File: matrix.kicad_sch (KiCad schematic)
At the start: 150 parts, among them SW10 SW_Push, SW11 SW_Push, SW12 SW_Push, SW13 SW_Push, SW14 SW_Push, SW15 SW_Push, SW16 SW_Push, SW17 SW_Push, SW18 SW_Push, SW19 SW_Push, SW2 SW_Push, SW20 SW_Push, SW21 SW_Push, SW22 SW_Push, SW23 SW_Push, SW24 SW_Push, SW25 SW_Push, SW26 SW_Push, SW27 SW_Push, SW28 SW_Push, SW29 SW_Push, SW3 SW_Push, SW30 SW_Push, SW31 SW_Push, SW32 SW_Push, SW33 SW_Push, SW34 SW_Push, SW35 SW_Push, SW36 SW_Push, SW37 SW_Push, SW38 SW_Push, SW39 SW_Push, SW4 SW_Push, SW40 SW_Push, SW41 SW_Push, SW42 SW_Push, SW43 SW_Push, SW44 SW_Push, SW45 SW_Push, SW46 SW_Push, SW47 SW_Push, SW48 SW_Push, SW49 SW_Push, SW5 SW_Push, SW50 SW_Push, SW51 SW_Push, SW52 SW_Push, SW53 SW_Push, SW54 SW_Push, SW55 SW_Push, SW56 SW_Push, SW57 SW_Push, SW58 SW_Push, SW59 SW_Push, SW6 SW_Push, SW60 SW_Push, SW61 SW_Push, SW62 SW_Push, SW63 SW_Push, SW64 SW_Push, SW65 SW_Push, SW66 SW_Push, SW67 SW_Push, SW68 SW_Push, SW69 SW_Push, SW7 SW_Push, SW70 SW_Push, SW71 SW_Push, SW72 SW_Push, SW73 SW_Push, SW74 SW_Push, SW75 SW_Push, SW76 SW_Push, SW8 SW_Push, SW9 SW_Push

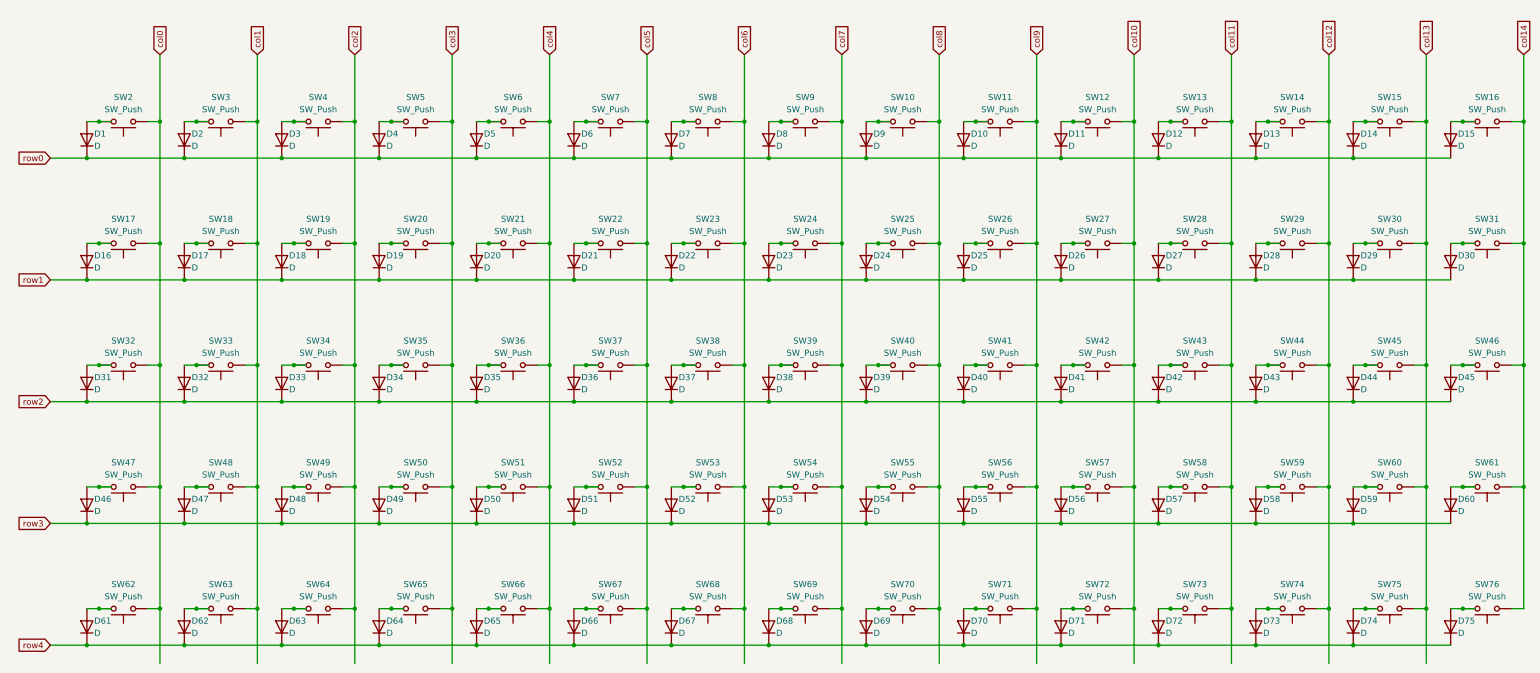
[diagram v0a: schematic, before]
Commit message: Matrix Design and slight keycap config
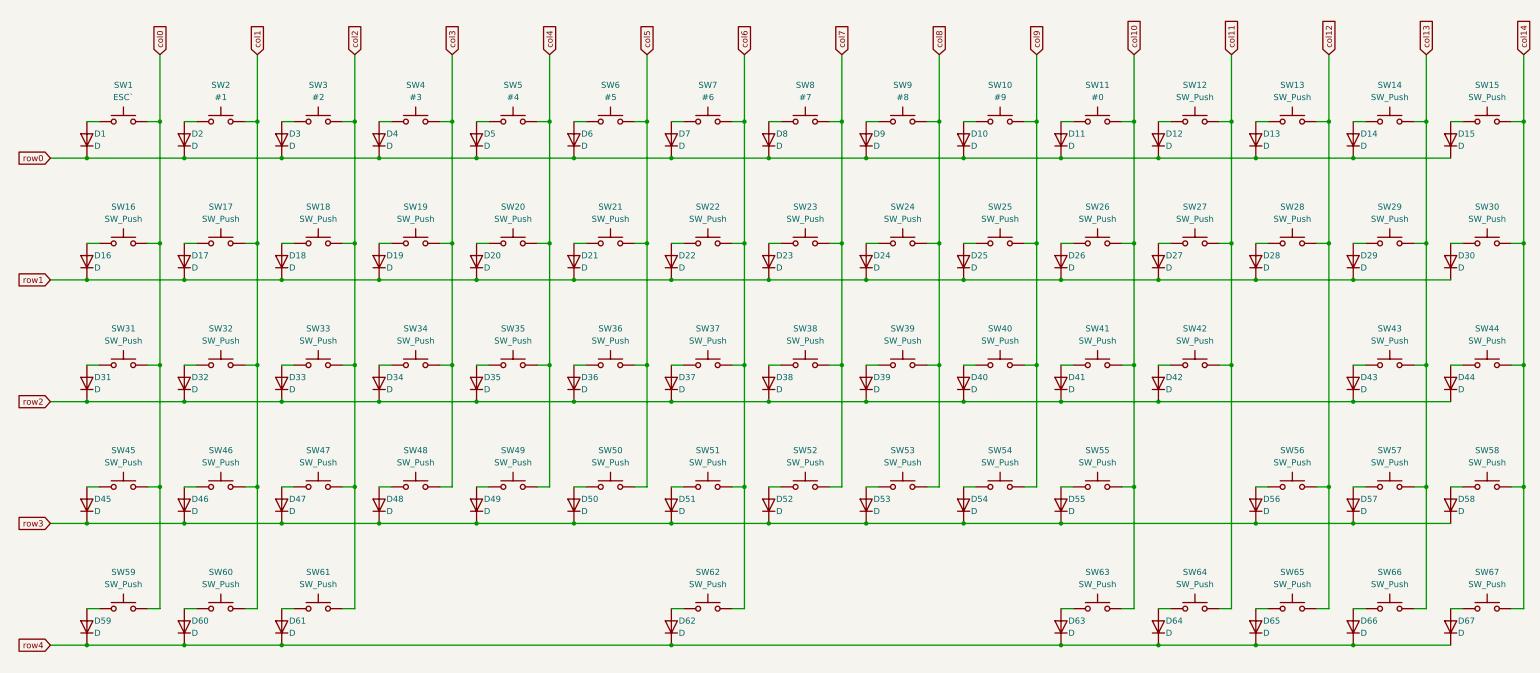
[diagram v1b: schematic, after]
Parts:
- removed D68, D69, D70, D71, D72, D73, D74, D75: D, symbol Device:D
- removed SW68, SW69, SW70, SW71, SW72, SW73, SW74, SW75, SW76: SW_Push, symbol Switch:SW_Push
- added SW2: #1, symbol Switch:SW_Push
- SW1: renamed from SW2; value SW_Push -> ESC`
- SW10: value SW_Push -> #9
- SW11: value SW_Push -> #0
- SW3: value SW_Push -> #2
- SW4: value SW_Push -> #3
- SW5: value SW_Push -> #4
- SW6: value SW_Push -> #5
- SW7: value SW_Push -> #6
- SW8: value SW_Push -> #7
- SW9: value SW_Push -> #8
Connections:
- net col0: now also SW1.2, SW16.2, SW31.2, SW45.2, SW59.2; no longer SW1.1, SW17.1, SW32.1, SW47.1, SW62.1
- net col1: now also SW17.2, SW32.2, SW46.2, SW60.2, SW2.2; no longer SW18.1, SW3.1, SW33.1, SW48.1, SW63.1
- net col10: now also SW11.2, SW26.2, SW41.2, SW55.2, SW63.2; no longer SW12.1, SW27.1, SW42.1, SW57.1
- net col11: now also SW12.2, SW27.2, SW42.2, SW64.2; no longer SW13.1, SW28.1, SW43.1, SW58.1
- net col12: now also SW13.2, SW28.2, SW56.2, SW65.2; no longer SW14.1, SW29.1, SW44.1, SW59.1
- net col13: now also SW14.2, SW29.2, SW43.2, SW57.2, SW66.2; no longer SW15.1, SW30.1, SW45.1, SW60.1
- net col14: now also SW15.2, SW30.2, SW44.2, SW58.2, SW67.2; no longer SW16.1, SW31.1, SW46.1, SW61.1
- net col2: now also SW18.2, SW3.2, SW33.2, SW47.2, SW61.2; no longer SW19.1, SW34.1, SW4.1, SW49.1, SW64.1
- net col3: now also SW19.2, SW34.2, SW4.2, SW48.2; no longer SW20.1, SW35.1, SW5.1, SW50.1, SW65.1
- net col4: now also SW20.2, SW35.2, SW49.2, SW5.2; no longer SW21.1, SW36.1, SW51.1, SW6.1, SW66.1
- net col5: now also SW21.2, SW36.2, SW50.2, SW6.2; no longer SW22.1, SW37.1, SW52.1, SW67.1, SW7.1
- net col6: now also SW22.2, SW37.2, SW51.2, SW62.2, SW7.2; no longer SW23.1, SW38.1, SW53.1, SW8.1
- net col7: now also SW23.2, SW38.2, SW52.2, SW8.2; no longer SW24.1, SW39.1, SW54.1, SW9.1
- net col8: now also SW24.2, SW39.2, SW53.2, SW9.2; no longer SW10.1, SW25.1, SW40.1, SW55.1
- net col9: now also SW10.2, SW25.2, SW40.2, SW54.2; no longer SW11.1, SW26.1, SW41.1, SW56.1
- net row2: no longer D45.1 (K)
- net row3: now also D45.1 (K); no longer D59.1 (K), D60.1 (K)
- net row4: now also D59.1 (K), D60.1 (K)
- net at D49.2 (A): now also SW49.1; no longer SW50.2
- net at D14.2 (A): now also SW14.1; no longer SW15.2
- net at D15.2 (A): now also SW15.1; no longer SW16.2
- net at D50.2 (A): now also SW50.1; no longer SW51.2
- net at D65.2 (A): now also SW65.1; no longer SW66.2
- net at D16.2 (A): now also SW16.1; no longer SW17.2
- net at D63.2 (A): now also SW63.1; no longer SW64.2
- net at D45.2 (A): now also SW45.1; no longer SW46.2
- net at D30.2 (A): now also SW30.1; no longer SW31.2
- net at D56.2 (A): now also SW56.1; no longer SW57.2
- net at D7.2 (A): now also SW7.1; no longer SW8.2
- net at D5.2 (A): now also SW5.1; no longer SW6.2
- net at D43.2 (A): now also SW43.1; no longer SW44.2
- net at D33.2 (A): now also SW33.1; no longer SW34.2
- net at D19.2 (A): now also SW19.1; no longer SW20.2
- net at D27.2 (A): now also SW27.1; no longer SW28.2
- net at D17.2 (A): now also SW17.1; no longer SW18.2
- net at D57.2 (A): now also SW57.1; no longer SW58.2
- net at D39.2 (A): now also SW39.1; no longer SW40.2
- net at D4.2 (A): now also SW4.1; no longer SW5.2
- net at D18.2 (A): now also SW18.1; no longer SW19.2
- net at D9.2 (A): now also SW9.1; no longer SW10.2
- net at D42.2 (A): now also SW42.1; no longer SW43.2
- net at D59.2 (A): now also SW59.1; no longer SW60.2
- net at D40.2 (A): now also SW40.1; no longer SW41.2
- net at D6.2 (A): now also SW6.1; no longer SW7.2
- net at D55.2 (A): now also SW55.1; no longer SW56.2
- net at D44.2 (A): now also SW44.1; no longer SW45.2
- net at D1.2 (A): now also SW1.1; no longer SW1.2
- net at D66.2 (A): now also SW66.1; no longer SW67.2
- net at D11.2 (A): now also SW11.1; no longer SW12.2
- net at D62.2 (A): now also SW62.1; no longer SW63.2
- net at D52.2 (A): now also SW52.1; no longer SW53.2
- net at D26.2 (A): now also SW26.1; no longer SW27.2
- net at D29.2 (A): now also SW29.1; no longer SW30.2
- net at D2.2 (A): now also SW2.1; no longer SW3.2
- net at D12.2 (A): now also SW12.1; no longer SW13.2
- net at D60.2 (A): now also SW60.1; no longer SW61.2
- net at D38.2 (A): now also SW38.1; no longer SW39.2
- net at D67.2 (A): now also SW67.1
- net at D28.2 (A): now also SW28.1; no longer SW29.2
- net at D20.2 (A): now also SW20.1; no longer SW21.2
- net at D36.2 (A): now also SW36.1; no longer SW37.2
- net at D31.2 (A): now also SW31.1; no longer SW32.2
- net at D21.2 (A): now also SW21.1; no longer SW22.2
- net at D3.2 (A): now also SW3.1; no longer SW4.2
- net at D47.2 (A): now also SW47.1; no longer SW48.2
- net at D25.2 (A): now also SW25.1; no longer SW26.2
- net at D48.2 (A): now also SW48.1; no longer SW49.2
- net at D13.2 (A): now also SW13.1; no longer SW14.2
- net at D41.2 (A): now also SW41.1; no longer SW42.2
- net at D37.2 (A): now also SW37.1; no longer SW38.2
- net at D24.2 (A): now also SW24.1; no longer SW25.2
- net at D64.2 (A): now also SW64.1; no longer SW65.2
- net at D34.2 (A): now also SW34.1; no longer SW35.2
- net at D35.2 (A): now also SW35.1; no longer SW36.2
- net at D10.2 (A): now also SW10.1; no longer SW11.2
- net at D54.2 (A): now also SW54.1; no longer SW55.2
- net at D61.2 (A): now also SW61.1; no longer SW62.2
- net at D46.2 (A): now also SW46.1; no longer SW47.2
- net at D22.2 (A): now also SW22.1; no longer SW23.2
- net at D51.2 (A): now also SW51.1; no longer SW52.2
- net at D8.2 (A): now also SW8.1; no longer SW9.2
- net at D58.2 (A): now also SW58.1; no longer SW59.2
- net at D23.2 (A): now also SW23.1; no longer SW24.2
- net at D32.2 (A): now also SW32.1; no longer SW33.2
- net at D53.2 (A): now also SW53.1; no longer SW54.2
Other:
- moved on the sheet: SW1

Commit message: Matrix Design Done
still need to assign footprints
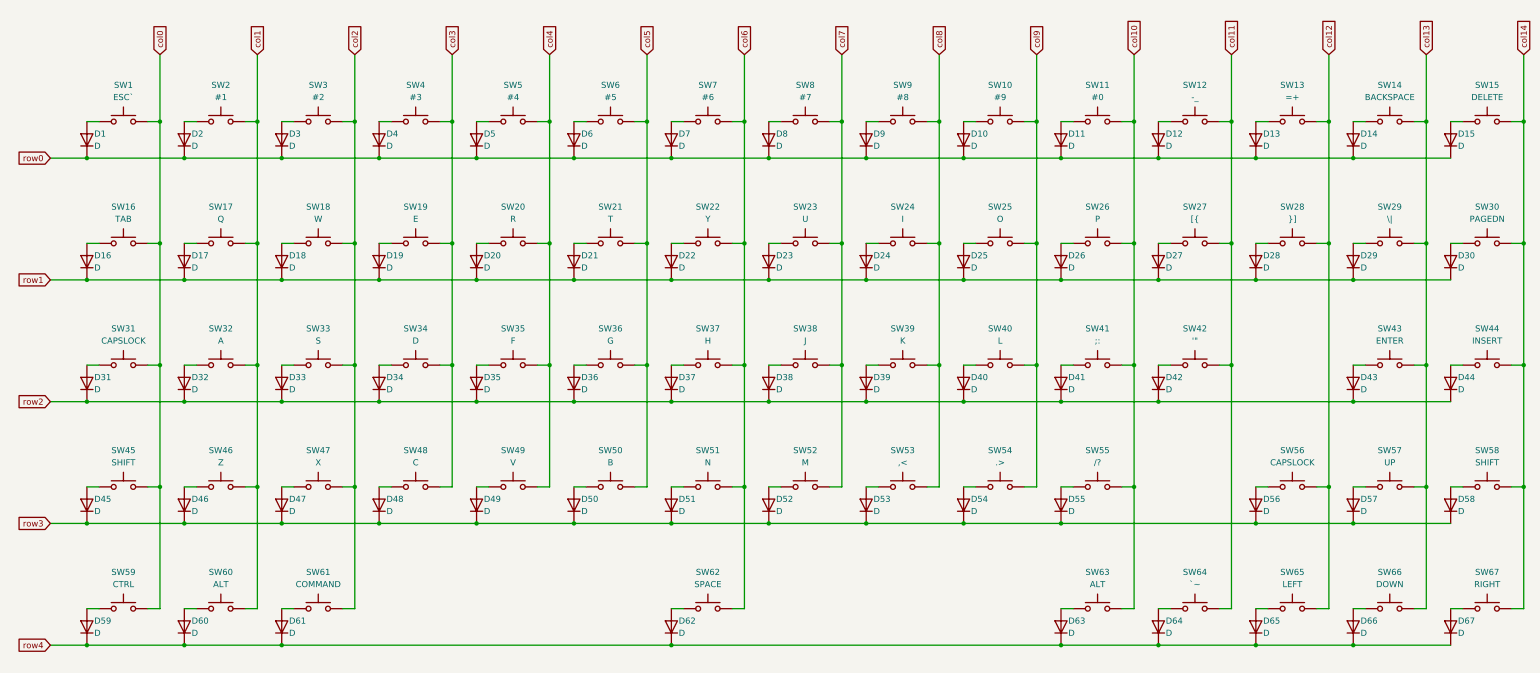
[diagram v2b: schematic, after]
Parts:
- SW12: value SW_Push -> -_
- SW13: value SW_Push -> =+
- SW14: value SW_Push -> BACKSPACE
- SW15: value SW_Push -> DELETE
- SW16: value SW_Push -> TAB
- SW17: value SW_Push -> Q
- SW18: value SW_Push -> W
- SW19: value SW_Push -> E
- SW20: value SW_Push -> R
- SW21: value SW_Push -> T
- SW22: value SW_Push -> Y
- SW23: value SW_Push -> U
- SW24: value SW_Push -> I
- SW25: value SW_Push -> O
- SW26: value SW_Push -> P
- SW27: value SW_Push -> [{
- SW28: value SW_Push -> }]
- SW29: value SW_Push -> \|
- SW30: value SW_Push -> PAGEDN
- SW31, SW56: value SW_Push -> CAPSLOCK
- SW32: value SW_Push -> A
- SW33: value SW_Push -> S
- SW34: value SW_Push -> D
- SW35: value SW_Push -> F
- SW36: value SW_Push -> G
- SW37: value SW_Push -> H
- SW38: value SW_Push -> J
- SW39: value SW_Push -> K
- SW40: value SW_Push -> L
- SW41: value SW_Push -> ;:
- SW42: value SW_Push -> '"
- SW43: value SW_Push -> ENTER
- SW44: value SW_Push -> INSERT
- SW45, SW58: value SW_Push -> SHIFT
- SW46: value SW_Push -> Z
- SW47: value SW_Push -> X
- SW48: value SW_Push -> C
- SW49: value SW_Push -> V
- SW50: value SW_Push -> B
- SW51: value SW_Push -> N
- SW52: value SW_Push -> M
- SW53: value SW_Push -> ,<
- SW54: value SW_Push -> .>
- SW55: value SW_Push -> /?
- SW57: value SW_Push -> UP
- SW59: value SW_Push -> CTRL
- SW60, SW63: value SW_Push -> ALT
- SW61: value SW_Push -> COMMAND
- SW62: value SW_Push -> SPACE
- SW64: value SW_Push -> `~
- SW65: value SW_Push -> LEFT
- SW66: value SW_Push -> DOWN
- SW67: value SW_Push -> RIGHT
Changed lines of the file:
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@@
 			)
 		)
-		(property "Value" "SW_Push"
+		(property "Value" "PAGEDN"
 			(at 341.63 67.31 0)
 			(effects
@@
 			)
 		)
-		(property "Value" "SW_Push"
+		(property "Value" "E"
 			(at 118.11 67.31 0)
 			(effects
@@
 			)
 		)
-		(property "Value" "SW_Push"
+		(property "Value" "Z"
 			(at 77.47 118.11 0)
 			(effects
@@
 			)
 		)
-		(property "Value" "SW_Push"
+		(property "Value" "=+"
 			(at 300.99 41.91 0)
 			(effects
@@
 			)
 		)
-		(property "Value" "SW_Push"
+		(property "Value" "RIGHT"
 			(at 341.63 143.51 0)
 			(effects
@@
 			)
 		)
-		(property "Value" "SW_Push"
+		(property "Value" "I"
 			(at 219.71 67.31 0)
 			(effects
@@
 			)
 		)
-		(property "Value" "SW_Push"
+		(property "Value" "INSERT"
 			(at 341.63 92.71 0)
 			(effects
@@
 			)
 		)
-		(property "Value" "SW_Push"
+		(property "Value" "SHIFT"
 			(at 341.63 118.11 0)
 			(effects
@@
 			)
 		)
-		(property "Value" "SW_Push"
+		(property "Value" "V"
 			(at 138.43 118.11 0)
 			(effects
@@
 			)
 		)
-		(property "Value" "SW_Push"
+		(property "Value" "\\|"
 			(at 321.31 67.31 0)
 			(effects
@@
 			)
 		)
-		(property "Value" "SW_Push"
+		(property "Value" "}]"
 			(at 300.99 67.31 0)
 			(effects
@@
 			)
 		)
-		(property "Value" "SW_Push"
+		(property "Value" "SHIFT"
 			(at 57.15 118.11 0)
 			(effects
@@
 			)
 		)
-		(property "Value" "SW_Push"
+		(property "Value" "A"
 			(at 77.47 92.71 0)
 			(effects
@@
 			)
 		)
-		(property "Value" "SW_Push"
+		(property "Value" ",<"
 			(at 219.71 118.11 0)
 			(effects
@@
 			)
 		)
-		(property "Value" "SW_Push"
+		(property "Value" "J"
 			(at 199.39 92.71 0)
 			(effects
@@
 			)
 		)
-		(property "Value" "SW_Push"
+		(property "Value" "CAPSLOCK"
 			(at 57.15 92.71 0)
 			(effects
@@
 			)
 		)
-		(property "Value" "SW_Push"
+		(property "Value" "COMMAND"
 			(at 97.79 143.51 0)
 			(effects
@@
 			)
 		)
-		(property "Value" "SW_Push"
+		(property "Value" "ALT"
 			(at 260.35 143.51 0)
 			(effects
@@
 			)
 		)
-		(property "Value" "SW_Push"
+		(property "Value" "U"
 			(at 199.39 67.31 0)
 			(effects
@@
 			)
 		)
-		(property "Value" "SW_Push"
+		(property "Value" ".>"
 			(at 240.03 118.11 0)
 			(effects
@@
 			)
 		)
-		(property "Value" "SW_Push"
+		(property "Value" "L"
 			(at 240.03 92.71 0)
 			(effects
@@
 			)
 		)
-		(property "Value" "SW_Push"
+		(property "Value" "ENTER"
 			(at 321.31 92.71 0)
 			(effects
@@
 			)
 		)
-		(property "Value" "SW_Push"
+		(property "Value" "TAB"
 			(at 57.15 67.31 0)
 			(effects
@@
 			)
 		)
-		(property "Value" "SW_Push"
+		(property "Value" "W"
 			(at 97.79 67.31 0)
 			(effects
@@
 			)
 		)
-		(property "Value" "SW_Push"
+		(property "Value" "S"
 			(at 97.79 92.71 0)
 			(effects
@@
 			)
 		)
-		(property "Value" "SW_Push"
+		(property "Value" "[{"
 			(at 280.67 67.31 0)
 			(effects
@@
 			)
 		)
-		(property "Value" "SW_Push"
+		(property "Value" "Q"
 			(at 77.47 67.31 0)
 			(effects
@@
 			)
 		)
-		(property "Value" "SW_Push"
+		(property "Value" "UP"
 			(at 321.31 118.11 0)
 			(effects
@@
 			)
 		)
-		(property "Value" "SW_Push"
+		(property "Value" "'\""
 			(at 280.67 92.71 0)
 			(effects
@@
 			)
 		)
-		(property "Value" "SW_Push"
+		(property "Value" "F"
 			(at 138.43 92.71 0)
 			(effects
@@
 			)
 		)
-		(property "Value" "SW_Push"
+		(property "Value" "T"
 			(at 158.75 67.31 0)
 			(effects
@@
 			)
 		)
-		(property "Value" "SW_Push"
+		(property "Value" ";:"
 			(at 260.35 92.71 0)
 			(effects
@@
 			)
 		)
-		(property "Value" "SW_Push"
+		(property "Value" "DOWN"
 			(at 321.31 143.51 0)
 			(effects
@@
 			)
 		)
-		(property "Value" "SW_Push"
+		(property "Value" "LEFT"
 			(at 300.99 143.51 0)
 			(effects
@@
 			)
 		)
-		(property "Value" "SW_Push"
+		(property "Value" "-_"
 			(at 280.67 41.91 0)
 			(effects
@@
 			)
 		)
-		(property "Value" "SW_Push"
+		(property "Value" "M"
 			(at 199.39 118.11 0)
 			(effects
@@
 			)
 		)
-		(property "Value" "SW_Push"
+		(property "Value" "CAPSLOCK"
 			(at 300.99 118.11 0)
 			(effects
@@
 			)
 		)
-		(property "Value" "SW_Push"
+		(property "Value" "B"
 			(at 158.75 118.11 0)
 			(effects
@@
 			)
 		)
-		(property "Value" "SW_Push"
+		(property "Value" "BACKSPACE"
 			(at 321.31 41.91 0)
 			(effects
@@
 			)
 		)
-		(property "Value" "SW_Push"
+		(property "Value" "K"
 			(at 219.71 92.71 0)
 			(effects
@@
 			)
 		)
-		(property "Value" "SW_Push"
+		(property "Value" "CTRL"
 			(at 57.15 143.51 0)
 			(effects
@@
 			)
 		)
-		(property "Value" "SW_Push"
+		(property "Value" "C"
 			(at 118.11 118.11 0)
 			(effects
@@
 			)
 		)
-		(property "Value" "SW_Push"
+		(property "Value" "G"
 			(at 158.75 92.71 0)
 			(effects
@@
 			)
 		)
-		(property "Value" "SW_Push"
+		(property "Value" "H"
 			(at 179.07 92.71 0)
 			(effects
@@
 			)
 		)
-		(property "Value" "SW_Push"
+		(property "Value" "O"
 			(at 240.03 67.31 0)
 			(effects
@@
 			)
 		)
-		(property "Value" "SW_Push"
+		(property "Value" "R"
 			(at 138.43 67.31 0)
 			(effects
@@
 			)
 		)
-		(property "Value" "SW_Push"
+		(property "Value" "X"
 			(at 97.79 118.11 0)
 			(effects
@@
 			)
 		)
-		(property "Value" "SW_Push"
+		(property "Value" "/?"
 			(at 260.35 118.11 0)
 			(effects
@@
 			)
 		)
-		(property "Value" "SW_Push"
+		(property "Value" "D"
 			(at 118.11 92.71 0)
 			(effects
@@
 			)
 		)
-		(property "Value" "SW_Push"
+		(property "Value" "DELETE"
 			(at 341.63 41.91 0)
 			(effects
@@
 			)
 		)
-		(property "Value" "SW_Push"
+		(property "Value" "`~"
 			(at 280.67 143.51 0)
 			(effects
@@
 			)
 		)
-		(property "Value" "SW_Push"
+		(property "Value" "SPACE"
 			(at 179.07 143.51 0)
 			(effects
@@
 			)
 		)
-		(property "Value" "SW_Push"
+		(property "Value" "Y"
 			(at 179.07 67.31 0)
 			(effects
@@
 			)
 		)
-		(property "Value" "SW_Push"
+		(property "Value" "N"
 			(at 179.07 118.11 0)
 			(effects
@@
 			)
 		)
-		(property "Value" "SW_Push"
+		(property "Value" "P"
 			(at 260.35 67.31 0)
 			(effects
@@
 			)
 		)
-		(property "Value" "SW_Push"
+		(property "Value" "ALT"
 			(at 77.47 143.51 0)
 			(effects

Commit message: Footprints Added
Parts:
- D1, D10, D11, D12, D13, D14, D15, D16, D17, D18, D19, D2, D20, D21, D22, D23, D24, D25, D26, D27, D28, D29, D3, D30, D31, D32, D33, D34, D35, D36, D37, D38, D39, D4, D40, D41, D42, D43, D44, D45, D46, D47, D48, D49, D5, D50, D51, D52, D53, D54, D55, D56, D57, D58, D59, D6, D60, D61, D62, D63, D64, D65, D66, D67, D7, D8, D9: footprint (none) -> Diode_SMD:D_SOD-123
- SW1, SW10, SW11, SW12, SW13, SW14, SW15, SW16, SW17, SW18, SW19, SW2, SW20, SW21, SW22, SW23, SW24, SW25, SW26, SW27, SW28, SW29, SW3, SW30, SW31, SW32, SW33, SW34, SW35, SW36, SW37, SW38, SW39, SW4, SW40, SW41, SW42, SW43, SW44, SW45, SW46, SW47, SW48, SW49, SW5, SW50, SW51, SW52, SW53, SW54, SW55, SW56, SW57, SW58, SW59, SW6, SW60, SW61, SW62, SW63, SW64, SW65, SW66, SW67, SW7, SW8, SW9: footprint (none) -> Alps_Only:ALPS-1U
